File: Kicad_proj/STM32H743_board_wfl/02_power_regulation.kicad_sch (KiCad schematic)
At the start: 2 parts, among them IC1 LT8609SEV#PBF, U4 TPS7A2033PDBVR

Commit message: v0.3 uzupelniony prebom + placement BMI088 na sch
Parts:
- renumbered IC1 to U1, U4 to U2
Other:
- moved on the sheet: U1, U2
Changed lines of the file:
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@@
 	(symbol
 		(lib_id "LT8609S:LT8609SEV#PBF")
-		(at 64.77 66.802 0)
+		(at 87.63 89.916 0)
 		(unit 1)
 		(body_style 1)
@@
 		(dnp no)
 		(fields_autoplaced yes)
-		(property "Reference" "IC1"
-			(at 80.01 59.69 0)
+		(property "Reference" "U1"
+			(at 102.87 82.55 0)
 			(show_name no)
 			(do_not_autoplace no)
@@
 		)
 		(property "Value" "LT8609SEV#PBF"
-			(at 80.01 62.23 0)
+			(at 102.87 85.09 0)
 			(show_name no)
 			(do_not_autoplace no)
@@
 		)
 		(property "Footprint" "LT8609SEVPBF"
-			(at 91.44 161.722 0)
+			(at 114.3 184.836 0)
 			(hide yes)
 			(show_name no)
@@
 		)
 		(property "Datasheet" "http://www.analog.com/media/en/technical-documentation/data-sheets/8609Sf.pdf"
-			(at 91.44 261.722 0)
+			(at 114.3 284.836 0)
 			(hide yes)
 			(show_name no)
@@
 		)
 		(property "Description" "42V, 2A/3A Peak Synchronous Step-Down Regulator with 2.5A Quiescent Current"
-			(at 64.77 66.802 0)
+			(at 87.63 89.916 0)
 			(hide yes)
 			(show_name no)
@@
 		)
 		(property "Height" "1"
-			(at 91.44 461.722 0)
+			(at 114.3 484.836 0)
 			(hide yes)
 			(show_name no)
@@
 		)
 		(property "Manufacturer_Name" "Analog Devices"
-			(at 91.44 561.722 0)
+			(at 114.3 584.836 0)
 			(hide yes)
 			(show_name no)
@@
 		)
 		(property "Manufacturer_Part_Number" "LT8609SEV#PBF"
-			(at 91.44 661.722 0)
+			(at 114.3 684.836 0)
 			(hide yes)
 			(show_name no)
@@
 		)
 		(property "Mouser Part Number" "584-LT8609SEVPBF"
-			(at 91.44 761.722 0)
+			(at 114.3 784.836 0)
 			(hide yes)
 			(show_name no)
@@
 		)
 		(property "Mouser Price/Stock" "https://www.mouser.co.uk/ProductDetail/Analog-Devices/LT8609SEVPBF?qs=BZBei1rCqCCvvHT89A2j%2FQ%3D%3D"
-			(at 91.44 861.722 0)
+			(at 114.3 884.836 0)
 			(hide yes)
 			(show_name no)
@@
 		)
 		(property "Arrow Part Number" "LT8609SEV#PBF"
-			(at 91.44 961.722 0)
+			(at 114.3 984.836 0)
 			(hide yes)
 			(show_name no)
@@
 		)
 		(property "Arrow Price/Stock" "https://www.arrow.com/en/products/lt8609sevpbf/analog-devices?utm_currency=USD&region=nac"
-			(at 91.44 1061.722 0)
+			(at 114.3 1084.836 0)
 			(hide yes)
 			(show_name no)
@@
 			(project "STM32H743_board_wfl"
 				(path "/3ffbaf01-8fe7-4f96-b685-21b9df9d548a/7e382ae8-ebae-4cf7-a9c0-9d94550a09cc"
-					(reference "IC1")
+					(reference "U1")
 					(unit 1)
 				)
@@
 	(symbol
 		(lib_id "Regulator_Linear:TPS7A20xxxDBV")
-		(at 144.526 124.968 0)
+		(at 221.996 91.948 0)
 		(unit 1)
 		(body_style 1)
@@
 		(dnp no)
 		(fields_autoplaced yes)
-		(property "Reference" "U4"
-			(at 144.526 115.062 0)
+		(property "Reference" "U2"
+			(at 221.996 81.28 0)
 			(show_name no)
 			(do_not_autoplace no)
@@
 		)
 		(property "Value" "TPS7A2033PDBVR"
-			(at 144.526 117.602 0)
+			(at 221.996 83.82 0)
 			(show_name no)
 			(do_not_autoplace no)
@@
 		)
 		(property "Footprint" "Package_TO_SOT_SMD:SOT-23-5"
-			(at 144.526 116.078 0)
+			(at 221.996 83.058 0)
 			(hide yes)
 			(show_name no)
@@
 		)
 		(property "Datasheet" "https://www.ti.com/lit/ds/symlink/tps7a20.pdf"
-			(at 144.526 112.268 0)
+			(at 221.996 79.248 0)
 			(hide yes)
 			(show_name no)
@@
 		)
 		(property "Description" "300 mA Low Dropout Voltage Regulator, Fixed Output, 1.6..6.0Vin, Low-Noise (7μV RMS), 6.5μA IQ LDO, SOT-23"
-			(at 144.526 124.968 0)
+			(at 221.996 91.948 0)
 			(hide yes)
 			(show_name no)
@@
 			(project "STM32H743_board_wfl"
 				(path "/3ffbaf01-8fe7-4f96-b685-21b9df9d548a/7e382ae8-ebae-4cf7-a9c0-9d94550a09cc"
-					(reference "U4")
+					(reference "U2")
 					(unit 1)
 				)

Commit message: v0.4b power smps
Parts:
- removed U2: TPS7A2033PDBVR, Package_TO_SOT_SMD:SOT-23-5, symbol Regulator_Linear:TPS7A20xxxDBV
- added C10, C6: 1uF, Capacitor_SMD:C_0603_1608Metric, symbol Device:C
- added C11, C9: 4.7uF, Capacitor_SMD:C_0603_1608Metric, symbol Device:C
- added C5: 10pF, Capacitor_SMD:C_01005_0402Metric, symbol Device:C
- added C7: 47uF, Capacitor_SMD:C_1206_3216Metric, symbol Device:C
- added C8: 10nF, Capacitor_SMD:C_01005_0402Metric, symbol Device:C
- added L1: SPM3020T-2R2M-LR, STM32H743_board_library_footprints:SPM3010-3020, symbol STM32H743_board_library_symbols:SPM3020T-2R2M-LR
- added R1: 100k, Resistor_SMD:R_01005_0402Metric, symbol Device:R
- added R2: 18.2k, Resistor_SMD:R_01005_0402Metric, symbol Device:R
- added R3: 1M, Resistor_SMD:R_01005_0402Metric, symbol Device:R
- added R4: 182k, Resistor_SMD:R_01005_0402Metric, symbol Device:R
- added U2: AP7361C-33E, Package_TO_SOT_SMD:SOT-223-3_TabPin2, symbol Regulator_Linear:AP7361C-33E
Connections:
- net at U1.1 (RT): now also R2.1
- net +26V_prefiltered: now reaches U1.10 (VIN_2)
- net +26V_prefiltered: now also U1.11 (EN/UV), U1.9 (VIN_1), C9.1
- net at U1.12 (PG): now also R1.2
- net at U1.13 (FB): now also C5.1, R3.1, R4.1
- net GND: now reaches U1.14 (GND_4)
- net GND: now also U1.17 (GND_5), U1.3 (GND_1), U1.4 (GND_2), U1.8 (GND_3), C10.2, C11.2, C6.2, C7.2, C8.2, C9.2, R2.2, R4.2, U2.2 (GND)
- net at U1.15 (TR/SS): now also C8.1
- net at U1.16 (SYNC): now also U1.2 (VCC), C6.1
- net at U1.5 (SW_1): now also U1.6 (SW_2), L1.2
- new net +3V3: C11.1, U2.3 (VO)
- new net +5V: C10.1, C5.2, C7.1, L1.1, R1.1, R3.2, U2.1 (VI)
- no-connect marks 0 -> 5

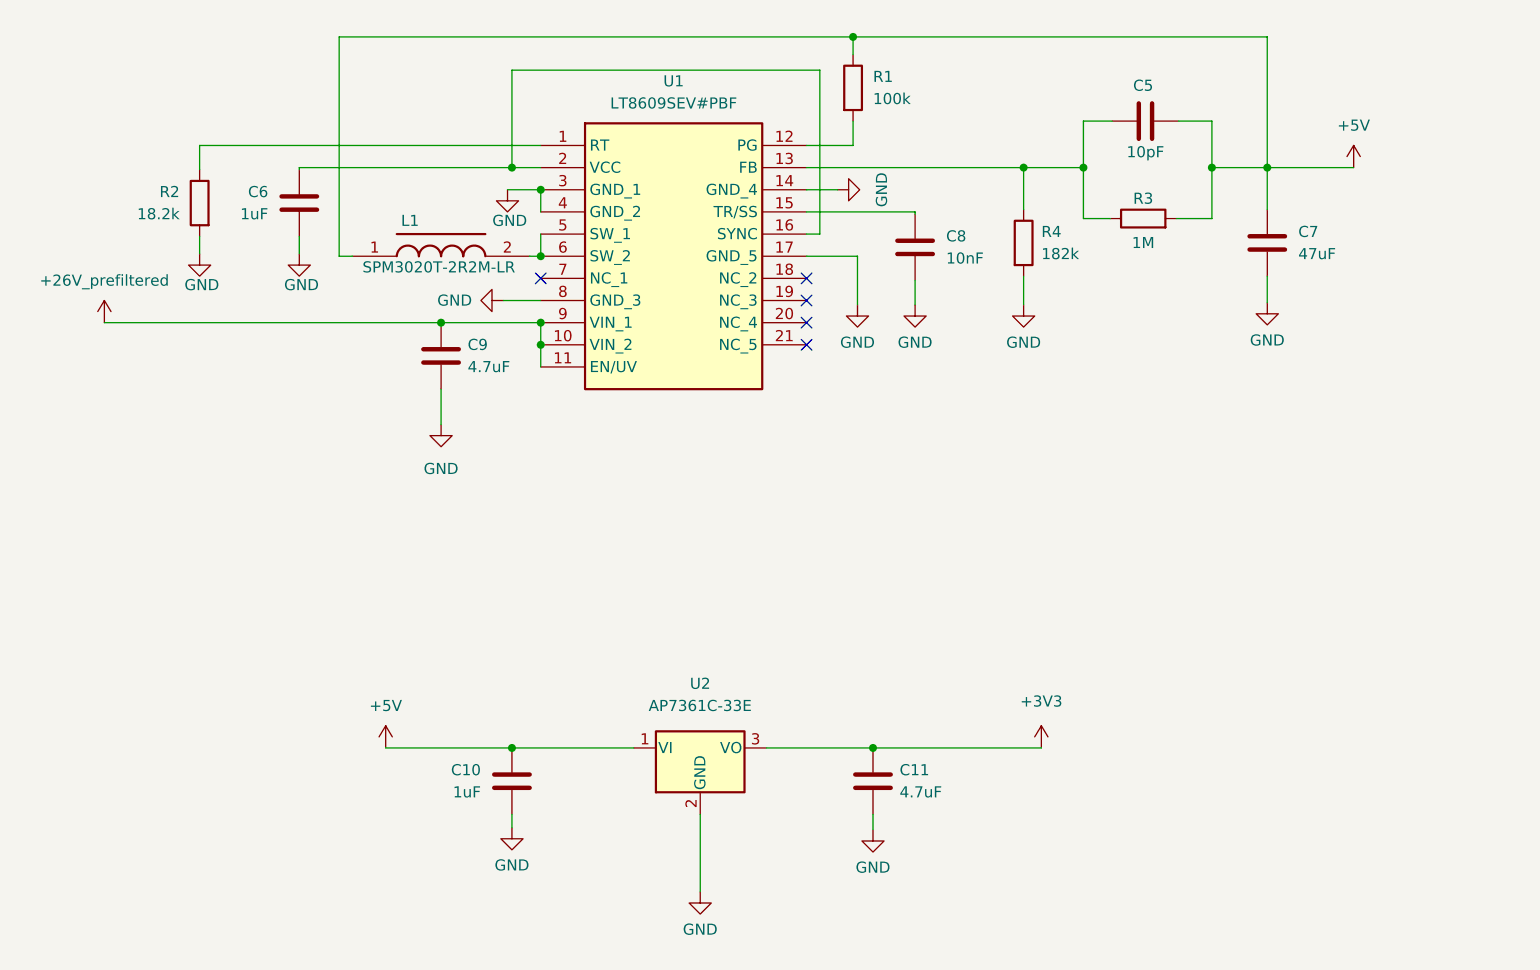
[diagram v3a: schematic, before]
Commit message: v0.5b tvs and stm32 vbat fixes
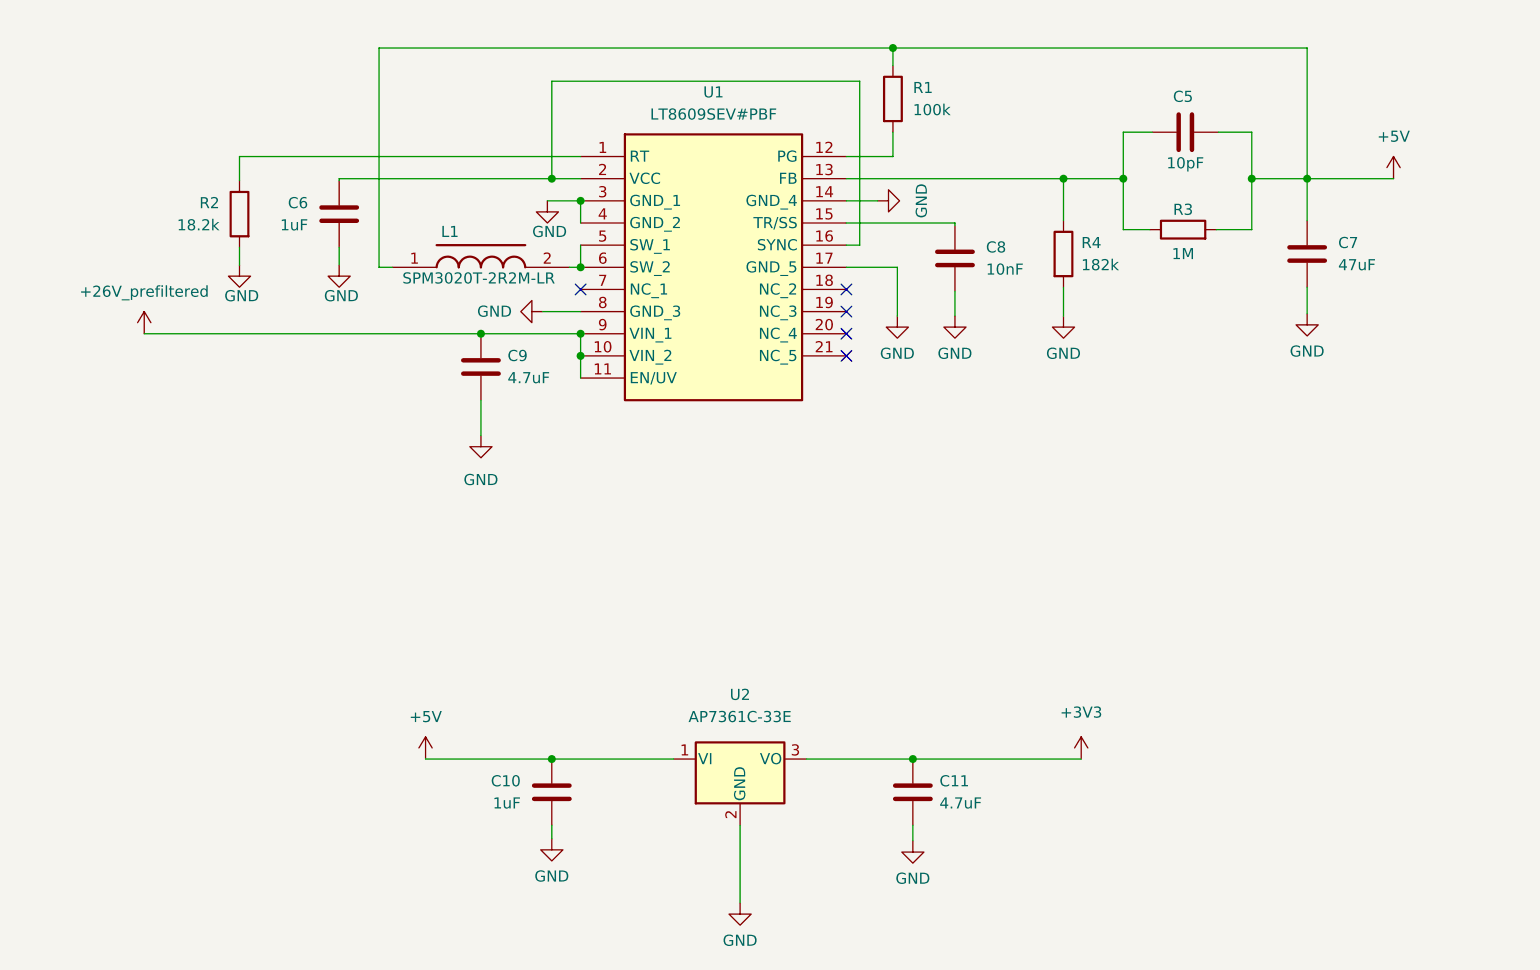
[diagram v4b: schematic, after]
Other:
- moved on the sheet: C10, C11, C5, C6, C7, C8, C9, L1, R1, R2, R3, R4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

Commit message: v0.5 footprint and lib fixes LT8609
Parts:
- U1: footprint LT8609SEVPBF -> STM32H743_board_library_footprints:LT8609SEVPBF; symbol LT8609S:LT8609SEV#PBF -> STM32H743_board_library_symbols:LT8609SEV#PBF; Description_1 (none) -> 42V, 2A/3A Peak Synchronous Step-Down Regulator with 2.5A Q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
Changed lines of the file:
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@@
 	)
 	(symbol
-		(lib_id "LT8609S:LT8609SEV#PBF")
+		(lib_id "STM32H743_board_library_symbols:LT8609SEV#PBF")
 		(at 123.19 65.278 0)
 		(unit 1)
@@
 		(fields_autoplaced yes)
 		(property "Reference" "U1"
-			(at 138.43 57.912 0)
+			(at 138.43 58.42 0)
 			(show_name no)
 			(do_not_autoplace no)
@@
 		)
 		(property "Value" "LT8609SEV#PBF"
-			(at 138.43 60.452 0)
+			(at 138.43 60.96 0)
 			(show_name no)
 			(do_not_autoplace no)
@@
 			)
 		)
-		(property "Footprint" "LT8609SEVPBF"
-			(at 149.86 160.198 0)
+		(property "Footprint" "STM32H743_board_library_footprints:LT8609SEVPBF"
+			(at 149.86 62.738 0)
 			(hide yes)
 			(show_name no)
@@
 					(size 1.27 1.27)
 				)
-				(justify left top)
+				(justify left)
 			)
 		)
 		(property "Datasheet" "http://www.analog.com/media/en/technical-documentation/data-sheets/8609Sf.pdf"
-			(at 149.86 260.198 0)
+			(at 149.86 65.278 0)
 			(hide yes)
 			(show_name no)
@@
 					(size 1.27 1.27)
 				)
-				(justify left top)
+				(justify left)
 			)
 		)
 		(property "Description" "42V, 2A/3A Peak Synchronous Step-Down Regulator with 2.5A Quiescent Current"
-			(at 123.19 65.278 0)
+			(at 135.382 53.086 0)
 			(hide yes)
 			(show_name no)
@@
 		)
 		(property "Height" "1"
-			(at 149.86 460.198 0)
+			(at 149.86 70.358 0)
 			(hide yes)
 			(show_name no)
@@
 					(size 1.27 1.27)
 				)
-				(justify left top)
+				(justify left)
 			)
 		)
 		(property "Manufacturer_Name" "Analog Devices"
-			(at 149.86 560.198 0)
+			(at 149.86 72.898 0)
 			(hide yes)
 			(show_name no)
@@
 					(size 1.27 1.27)
 				)
-				(justify left top)
+				(justify left)
 			)
 		)
 		(property "Manufacturer_Part_Number" "LT8609SEV#PBF"
-			(at 149.86 660.198 0)
+			(at 149.86 75.438 0)
 			(hide yes)
 			(show_name no)
@@
 					(size 1.27 1.27)
 				)
-				(justify left top)
+				(justify left)
 			)
 		)
 		(property "Mouser Part Number" "584-LT8609SEVPBF"
-			(at 149.86 760.198 0)
+			(at 149.86 77.978 0)
 			(hide yes)
 			(show_name no)
@@
 					(size 1.27 1.27)
 				)
-				(justify left top)
+				(justify left)
 			)
 		)
 		(property "Mouser Price/Stock" "https://www.mouser.co.uk/ProductDetail/Analog-Devices/LT8609SEVPBF?qs=BZBei1rCqCCvvHT89A2j%2FQ%3D%3D"
-			(at 149.86 860.198 0)
+			(at 149.86 80.518 0)
 			(hide yes)
 			(show_name no)
@@
 					(size 1.27 1.27)
 				)
-				(justify left top)
+				(justify left)
 			)
 		)
 		(property "Arrow Part Number" "LT8609SEV#PBF"
-			(at 149.86 960.198 0)
+			(at 149.86 83.058 0)
 			(hide yes)
 			(show_name no)
@@
 					(size 1.27 1.27)
 				)
-				(justify left top)
+				(justify left)
 			)
 		)
 		(property "Arrow Price/Stock" "https://www.arrow.com/en/products/lt8609sevpbf/analog-devices?utm_currency=USD&region=nac"
-			(at 149.86 1060.198 0)
+			(at 149.86 85.598 0)
 			(hide yes)
 			(show_name no)
@@
 					(size 1.27 1.27)
 				)
-				(justify left top)
+				(justify left)
 			)
 		)
+		(property "Description_1" "42V, 2A/3A Peak Synchronous Step-Down Regulator with 2.5A Quiescent Current"
+			(at 149.86 67.818 0)
+			(hide yes)
+			(show_name no)
+			(do_not_autoplace no)
+			(effects
+				(font
+					(size 1.27 1.27)
+				)
+				(justify left)
+			)
+		)

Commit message: SCH v0.6 LT8609 NC -> GND
remove floats according to datasheet
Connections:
- net GND: now also U1.18 (NC_2), U1.19 (NC_3), U1.20 (NC_4), U1.21 (NC_5), U1.7 (NC_1)
- no-connect marks 5 -> 0
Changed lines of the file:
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@@
+	)
+	(junction
+		(at 153.67 80.518)
+		(diameter 0)
+		(color 0 0 0 0)
 	)
 	(junction
@@
 	)
 	(junction
+		(at 153.67 83.058)
+		(diameter 0)
+		(color 0 0 0 0)
+	)
+	(junction
+		(at 153.67 77.978)
+		(diameter 0)
+		(color 0 0 0 0)
+	)
+	(junction
 		(at 119.888 134.366)
 		(diameter 0)
@@
 	)
 	(junction
+		(at 153.67 85.598)
+		(diameter 0)
+		(color 0 0 0 0)
+	)
+	(junction
 		(at 178.562 67.818)
 		(diameter 0)
@@
 		(color 0 0 0 0)
 	)
-	(no_connect
-		(at 153.67 85.598)
-	)
-	(no_connect
-		(at 153.67 88.138)
-	)
-	(no_connect
-		(at 123.19 80.518)
-	)
-	(no_connect
-		(at 153.67 80.518)
-	)
-	(no_connect
-		(at 153.67 83.058)
+	(junction
+		(at 123.19 83.058)
+		(diameter 0)
+		(color 0 0 0 0)
 	)
 	(wire
@@
 	(wire
 		(pts
+			(xy 153.67 85.598) (xy 153.67 88.138)
+		)
+		(stroke
+			(width 0)
+			(type default)
+		)
+	)
+	(wire
+		(pts
 			(xy 185.42 73.66) (xy 185.42 67.818)
 		)
@@
 	(wire
 		(pts
+			(xy 123.19 80.518) (xy 123.19 83.058)
+		)
+		(stroke
+			(width 0)
+			(type default)
+		)
+	)
+	(wire
+		(pts
 			(xy 153.67 70.358) (xy 157.226 70.358)
 		)
@@
 	(wire
 		(pts
+			(xy 153.67 83.058) (xy 153.67 85.598)
+		)
+		(stroke
+			(width 0)
+			(type default)
+		)
+	)
+	(wire
+		(pts
 			(xy 200.152 62.484) (xy 200.152 67.818)
 		)
@@
 	(wire
 		(pts
+			(xy 153.67 77.978) (xy 153.67 80.518)
+		)
+		(stroke
+			(width 0)
+			(type default)
+		)
+	)
+	(wire
+		(pts
 			(xy 166.116 72.898) (xy 166.116 73.152)
 		)
@@
 		)
 		(stroke
+			(width 0)
+			(type default)
+		)
+	)
+	(wire
+		(pts
+			(xy 153.67 80.518) (xy 153.67 83.058)
+		)
+		(stroke
